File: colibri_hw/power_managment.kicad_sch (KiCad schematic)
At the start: 9 parts

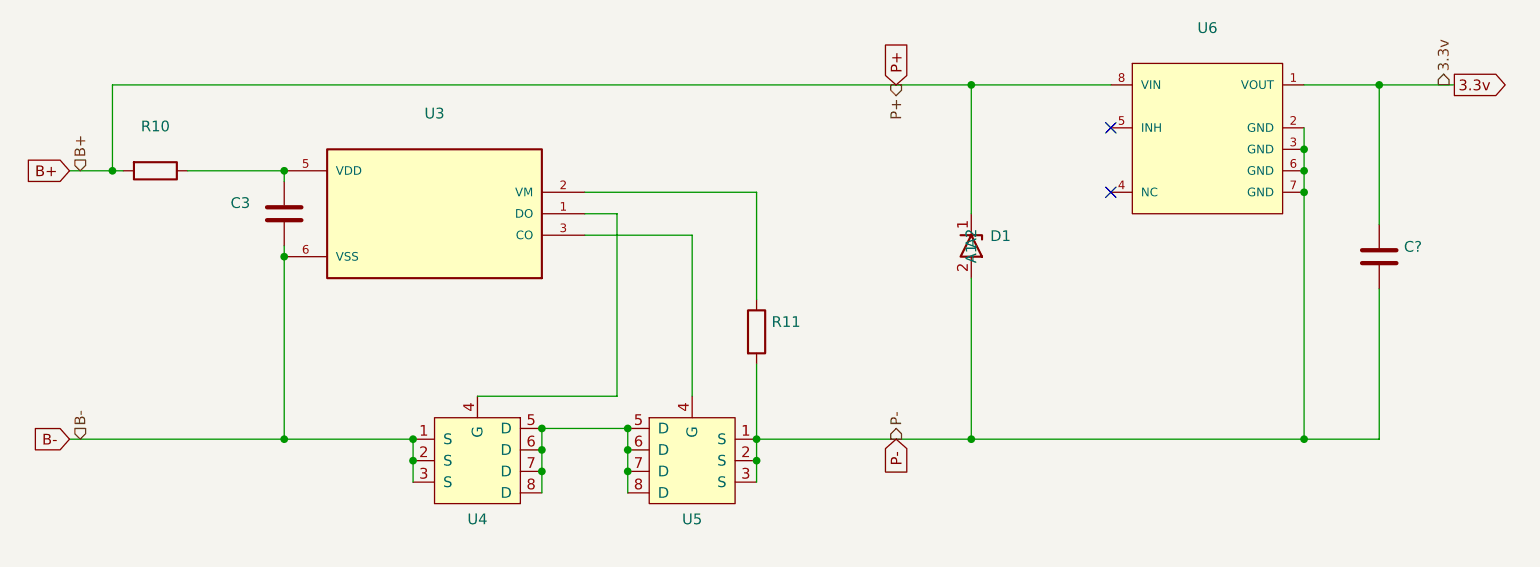
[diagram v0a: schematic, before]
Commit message: [v1.0.1]: Fix UART communication issues due to R5 value
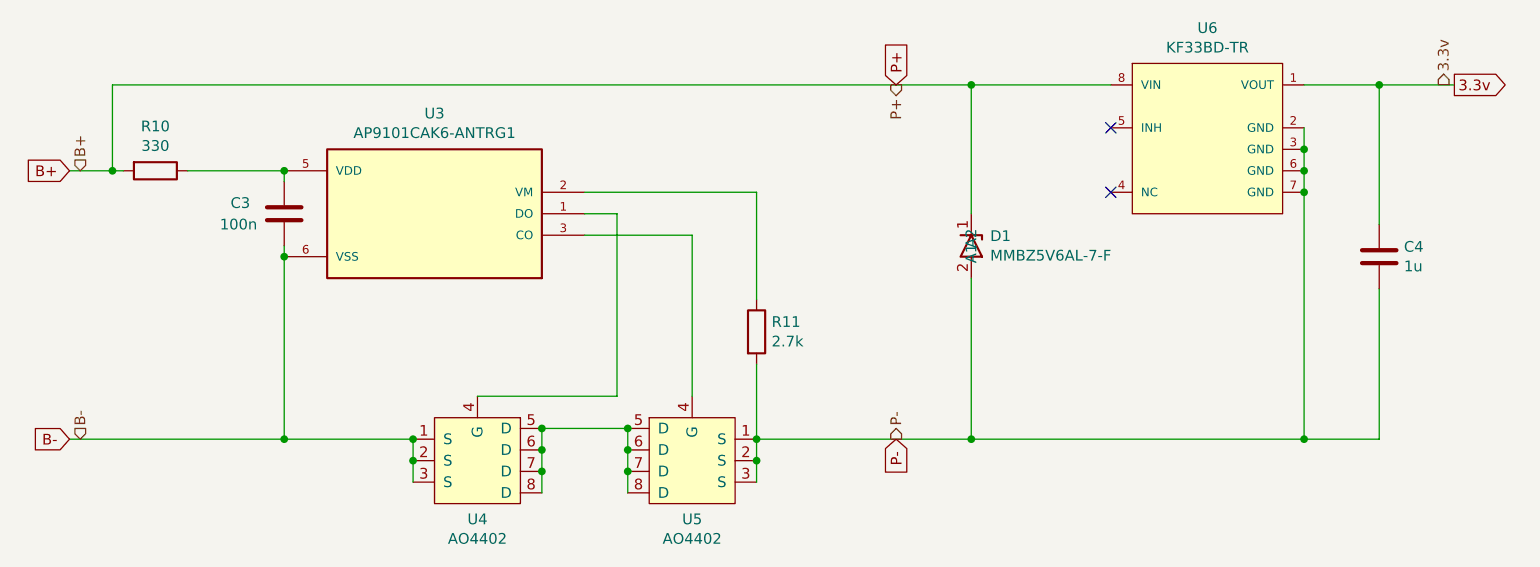
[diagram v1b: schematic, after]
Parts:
- C3: value (none) -> 100n; footprint (none) -> Capacitor_SMD:C_1206_3216Metric
- C4: renamed from C?; value (none) -> 1u; footprint (none) -> Capacitor_SMD:C_1206_3216Metric_Pad1.33x1.80mm_HandSolder
- D1: value (none) -> MMBZ5V6AL-7-F; footprint (none) -> Package_TO_SOT_SMD:SOT-23
- R10: value (none) -> 330; footprint (none) -> Resistor_SMD:R_0805_2012Metric
- R11: value (none) -> 2.7k; footprint (none) -> Resistor_SMD:R_0805_2012Metric
- U3: value (none) -> AP9101CAK6-ANTRG1; footprint (none) -> Package_TO_SOT_SMD:SOT-23-6
- U4, U5: value (none) -> AO4402; footprint (none) -> Package_SO:SOIC127P490X600X175-8N
- U6: value (none) -> KF33BD-TR; footprint (none) -> eec:STMicroelectronics-KF33BD-TR-Level_A
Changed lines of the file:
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@@
     (in_bom yes) (on_board yes)
     (property "Reference" "U3" (id 0) (at 116.84 71.9582 0))
-    (property "Value" "" (id 1) (at 116.84 74.2696 0))
-    (property "Footprint" "" (id 2) (at 116.84 83.82 0)
+    (property "Value" "AP9101CAK6-ANTRG1" (id 1) (at 116.84 74.2696 0))
+    (property "Footprint" "Package_TO_SOT_SMD:SOT-23-6" (id 2) (at 116.84 83.82 0)
       (effects (font (size 1.27 1.27)) (justify left bottom) hide)
     )
@@
     (in_bom yes) (on_board yes)
     (property "Reference" "U4" (id 0) (at 121.92 119.9642 90))
-    (property "Value" "" (id 1) (at 121.92 122.2756 90))
-    (property "Footprint" "" (id 2) (at 120.65 138.43 0)
+    (property "Value" "AO4402" (id 1) (at 121.92 122.2756 90))
+    (property "Footprint" "Package_SO:SOIC127P490X600X175-8N" (id 2) (at 120.65 138.43 0)
       (effects (font (size 1.27 1.27)) hide)
     )
@@
     (in_bom yes) (on_board yes)
     (property "Reference" "U5" (id 0) (at 147.32 119.9642 90))
-    (property "Value" "" (id 1) (at 147.32 122.2756 90))
-    (property "Footprint" "" (id 2) (at 148.59 138.43 0)
+    (property "Value" "AO4402" (id 1) (at 147.32 122.2756 90))
+    (property "Footprint" "Package_SO:SOIC127P490X600X175-8N" (id 2) (at 148.59 138.43 0)
       (effects (font (size 1.27 1.27)) hide)
     )
@@
       (effects (font (size 1.27 1.27)) (justify right))
     )
-    (property "Value" "" (id 1) (at 91.44 85.09 0)
+    (property "Value" "100n" (id 1) (at 91.44 85.09 0)
       (effects (font (size 1.27 1.27)) (justify right))
     )
-    (property "Footprint" "" (id 2) (at 98.0948 80.01 0)
+    (property "Footprint" "Capacitor_SMD:C_1206_3216Metric" (id 2) (at 98.0948 80.01 0)
       (effects (font (size 1.27 1.27)) hide)
     )
@@
       (effects (font (size 1.27 1.27)) (justify left))
     )
-    (property "Value" "" (id 1) (at 156.718 98.933 0)
+    (property "Value" "2.7k" (id 1) (at 156.718 98.933 0)
       (effects (font (size 1.27 1.27)) (justify left))
     )
-    (property "Footprint" "" (id 2) (at 153.162 97.79 90)
+    (property "Footprint" "Resistor_SMD:R_0805_2012Metric" (id 2) (at 153.162 97.79 90)
       (effects (font (size 1.27 1.27)) hide)
     )
@@
     (in_bom yes) (on_board yes)
     (property "Reference" "R10" (id 0) (at 83.82 73.4822 90))
-    (property "Value" "" (id 1) (at 83.82 75.7936 90))
-    (property "Footprint" "" (id 2) (at 83.82 76.962 90)
+    (property "Value" "330" (id 1) (at 83.82 75.7936 90))
+    (property "Footprint" "Resistor_SMD:R_0805_2012Metric" (id 2) (at 83.82 76.962 90)
       (effects (font (size 1.27 1.27)) hide)
     )
@@
   (symbol (lib_id "Device:C") (at 228.6 88.9 0) (unit 1)
     (in_bom yes) (on_board yes)
-    (property "Reference" "C?" (id 0) (at 231.521 87.7316 0)
+    (property "Reference" "C4" (id 0) (at 231.521 87.7316 0)
       (effects (font (size 1.27 1.27)) (justify left))
     )
-    (property "Value" "" (id 1) (at 231.521 90.043 0)
+    (property "Value" "1u" (id 1) (at 231.521 90.043 0)
       (effects (font (size 1.27 1.27)) (justify left))
     )
-    (property "Footprint" "" (id 2) (at 229.5652 92.71 0)
+    (property "Footprint" "Capacitor_SMD:C_1206_3216Metric_Pad1.33x1.80mm_HandSolder" (id 2) (at 229.5652 92.71 0)
       (effects (font (size 1.27 1.27)) hide)
     )
@@
       (effects (font (size 1.27 1.27)) (justify left))
     )
-    (property "Value" "" (id 1) (at 182.5752 88.773 90)
+    (property "Value" "MMBZ5V6AL-7-F" (id 1) (at 182.5752 88.773 90)
       (effects (font (size 1.27 1.27)) (justify left))
     )
-    (property "Footprint" "" (id 2) (at 182.88 87.63 0)
+    (property "Footprint" "Package_TO_SOT_SMD:SOT-23" (id 2) (at 182.88 87.63 0)
       (effects (font (size 1.27 1.27)) hide)
     )
@@
     (in_bom yes) (on_board yes)
     (property "Reference" "U6" (id 0) (at 208.28 61.849 0))
-    (property "Value" "" (id 1) (at 208.28 64.1604 0))
-    (property "Footprint" "" (id 2) (at 194.31 58.42 0)
+    (property "Value" "KF33BD-TR" (id 1) (at 208.28 64.1604 0))
+    (property "Footprint" "eec:STMicroelectronics-KF33BD-TR-Level_A" (id 2) (at 194.31 58.42 0)
       (effects (font (size 1.27 1.27)) (justify left) hide)
     )
